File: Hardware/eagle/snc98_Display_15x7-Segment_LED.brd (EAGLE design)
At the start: 154.9 x 33.5 mm, 72 parts, among them M10 IRLML2244, M11 IRLML2244, M4 IRLML2244, M5 IRLML2244, M6 IRLML2244, M7 IRLML2244, M8 IRLML2244, M9 IRLML2244, X1 MICROMATCH-12, X2 MICROMATCH-14, X3 MICROMATCH-12, X4 MICROMATCH-14

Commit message: snc98_main_cpu V1.0
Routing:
- net D14_A: track 36.1 -> 38.1 mm
- net D12_A: track 21.3 -> 22.9 mm
- net D3_A: track 27.9 -> 29.2 mm
- net D7_A: track 72.0 -> 73.3 mm
- net D5_A: track 44.7 -> 46.0 mm
- net D0_A: track 35.6 -> 36.9 mm
- net D4_A: track 33.4 -> 34.7 mm
- net D13_A: track 24.7 -> 26.0 mm
- net D8_A: track 55.0 -> 56.3 mm
- net D2_A: track 18.5 -> 19.8 mm
- net D9_A: track 37.9 -> 39.2 mm
- net D6_A: track 52.4 -> 53.7 mm
- net D11_A: track 23.8 -> 25.0 mm
- net D1_A: track 28.1 -> 29.3 mm
- net D10_A: track 30.8 -> 32.0 mm

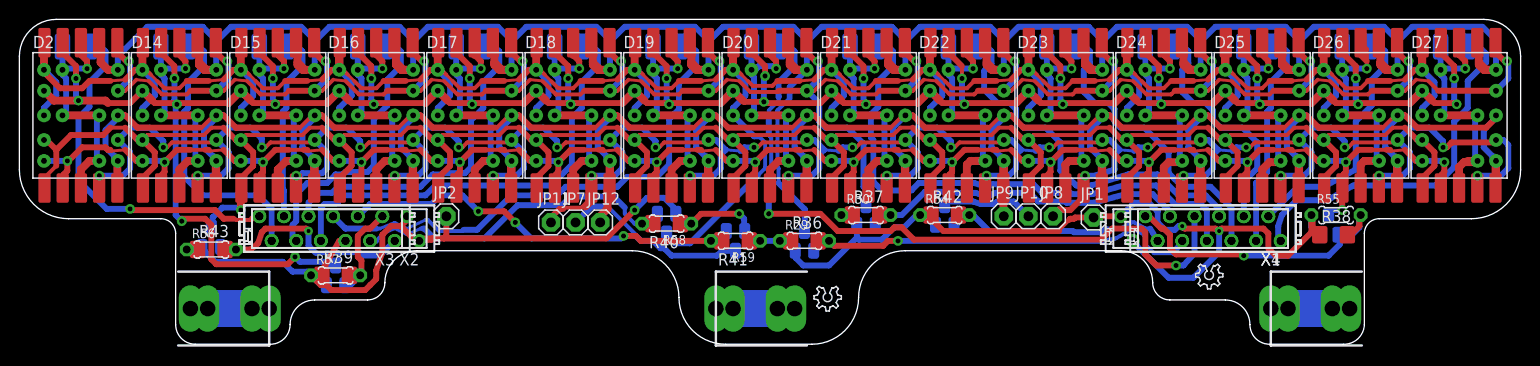
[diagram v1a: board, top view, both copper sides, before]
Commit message: Work like WIN_7 Calculator in "Standard Mode"
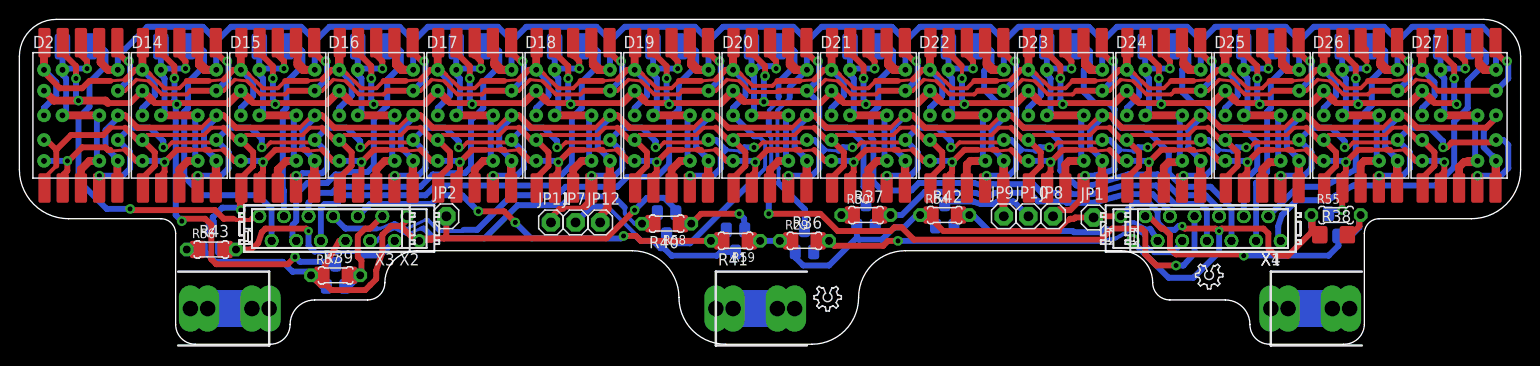
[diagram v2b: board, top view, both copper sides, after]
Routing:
- net IO-DP: track 42.6 -> 43.5 mm
- net CA_LED: track 192.9 -> 193.7 mm
